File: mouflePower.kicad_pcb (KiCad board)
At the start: 2 copper layers, 72.9 x 42.7 mm, 122 parts, among them J1 FTDI, J10 EINK, J11 ANALOG, J2 Antenna, J3 I2C, J4 ICSP, J5 V_MAIN, J6 Relay, J7 SPI, J8 I2C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

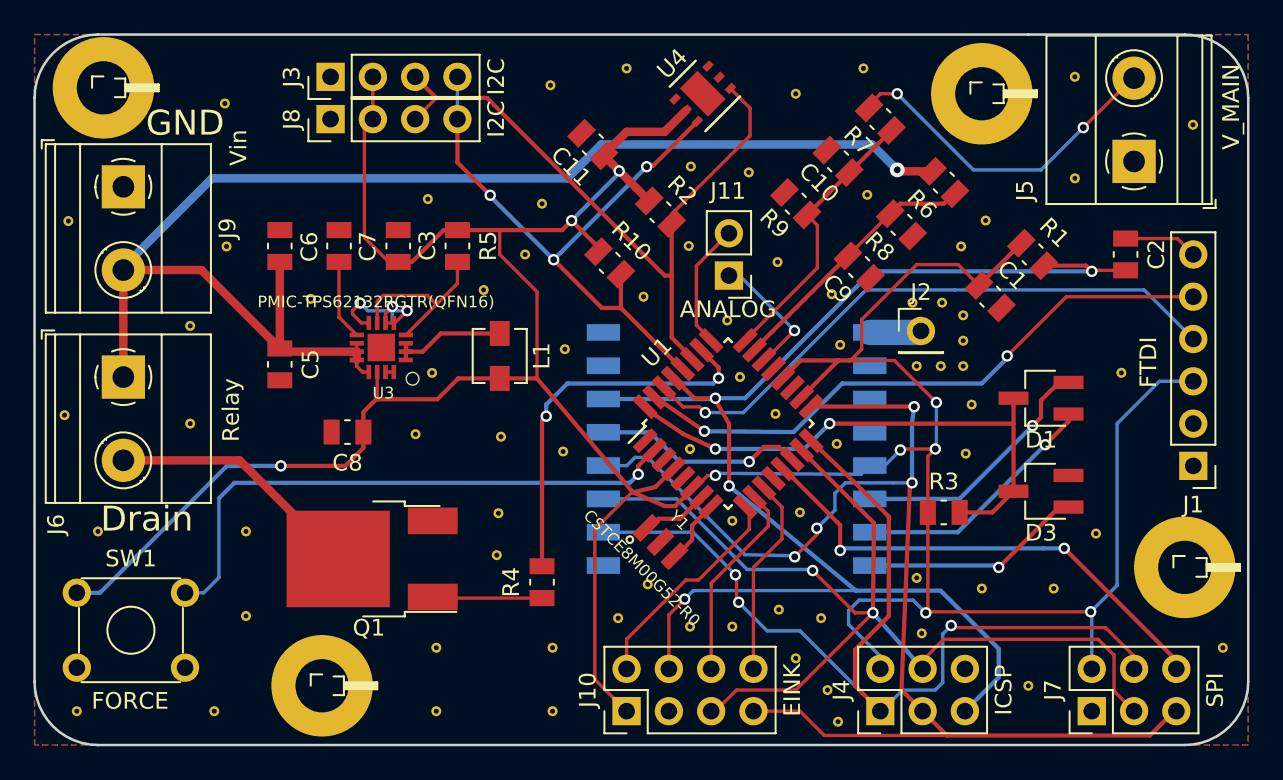
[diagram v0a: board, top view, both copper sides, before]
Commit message: Add flyback diode
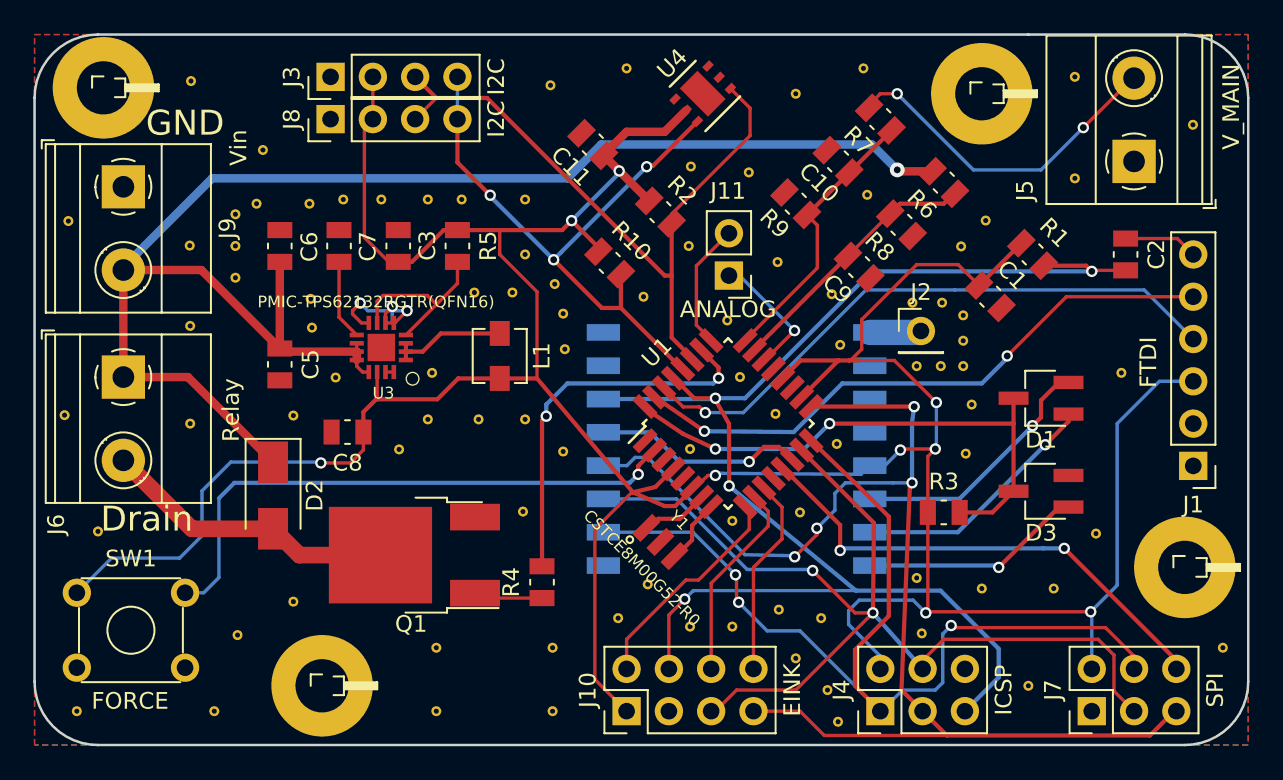
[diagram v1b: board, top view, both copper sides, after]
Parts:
- added D2: S1K-13-F, Diode_SMD:D_SMA, F.Cu at (113.4, 63.2)
- added REF**: VIA-GROUND, ViaGround:VIA-GROUND, F.Cu at (112.8, 42.5)
- added REF**: VIA-GROUND, ViaGround:VIA-GROUND, F.Cu at (119.9, 45.5)
- added REF**: VIA-GROUND, ViaGround:VIA-GROUND, F.Cu at (115.6, 45.7)
- added REF**: VIA-GROUND, ViaGround:VIA-GROUND, F.Cu at (112.4, 45.7)
- added REF**: VIA-GROUND, ViaGround:VIA-GROUND, F.Cu at (111.1, 46.4)
- added REF**: VIA-GROUND, ViaGround:VIA-GROUND, F.Cu at (108.4, 48.2)
- added REF**: VIA-GROUND, ViaGround:VIA-GROUND, F.Cu at (111.1, 50.2)
- added REF**: VIA-GROUND, ViaGround:VIA-GROUND, F.Cu at (115.7, 53.2)
- added REF**: VIA-GROUND, ViaGround:VIA-GROUND, F.Cu at (121.0, 60.5)
- added REF**: VIA-GROUND, ViaGround:VIA-GROUND, F.Cu at (117.1, 56.2)
- added REF**: VIA-GROUND, ViaGround:VIA-GROUND, F.Cu at (128.5, 58.7)
- added REF**: VIA-GROUND, ViaGround:VIA-GROUND, F.Cu at (130.8, 52.3)
- added REF**: VIA-GROUND, ViaGround:VIA-GROUND, F.Cu at (130.3, 50.5)
- added REF**: VIA-GROUND, ViaGround:VIA-GROUND, F.Cu at (127.8, 51.1)
- added REF**: VIA-GROUND, ViaGround:VIA-GROUND, F.Cu at (124.7, 45.5)
- added REF**: VIA-GROUND, ViaGround:VIA-GROUND, F.Cu at (117.6, 45.5)
- moved REF** 14.8 mm to (114.6, 58.4)
- moved REF** 5.09 mm to (114.6, 69.6)
- moved Q1 2.55 mm to (122.9, 66.8)
- moved REF** 2.44 mm to (108.5, 38.4)
- moved REF** 1.70 mm to (125.7, 58.7)
- moved REF** 1.48 mm to (128.4, 64.2)
- moved REF** 1.25 mm to (111.3, 71.6)
- moved REF** 1.15 mm to (122.7, 58.7)
- moved REF** 1.05 mm to (128.5, 45.5)
- moved REF** 0.58 mm to (125.5, 51.1)
- moved REF** 0.53 mm to (111.1, 48.3)
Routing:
- net +VDC: track 82.4 -> 93.5 mm
- net Net-(Q1-Pad1): track 6.59 -> 4.15 mm
- net /Drain: track 15.4 -> 17.8 mm
- net +3V3: track 216.8 -> 218.5 mm
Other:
- net class Drain added: clearance 0.2032, trace_width 1, via_dia 0.6858, via_drill 0.4064
